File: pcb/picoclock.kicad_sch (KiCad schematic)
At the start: 59 parts, among them J1 UART, J10 USB, J11 Alt Power, J12 PWM, J2 AUDIO, J3 xx, J4 xx, J5 Micro_SD_Card_Det1, J6 USB_C_Receptacle, J7 xx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

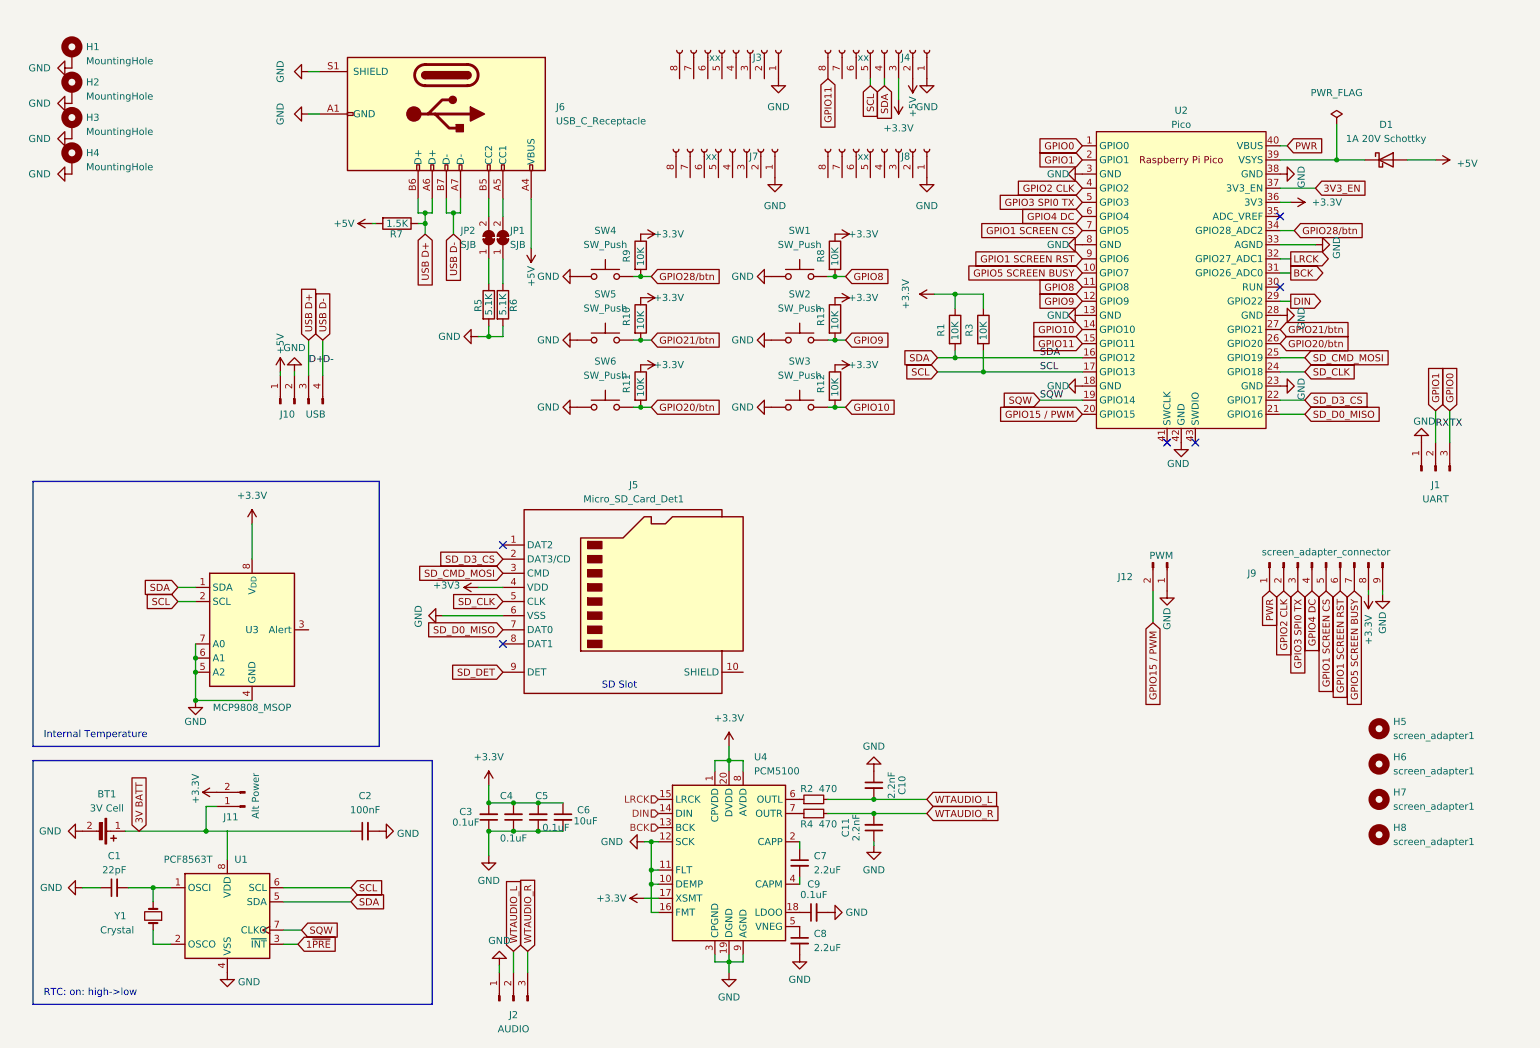
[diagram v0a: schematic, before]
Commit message: [pcb] new GPIO arrangement
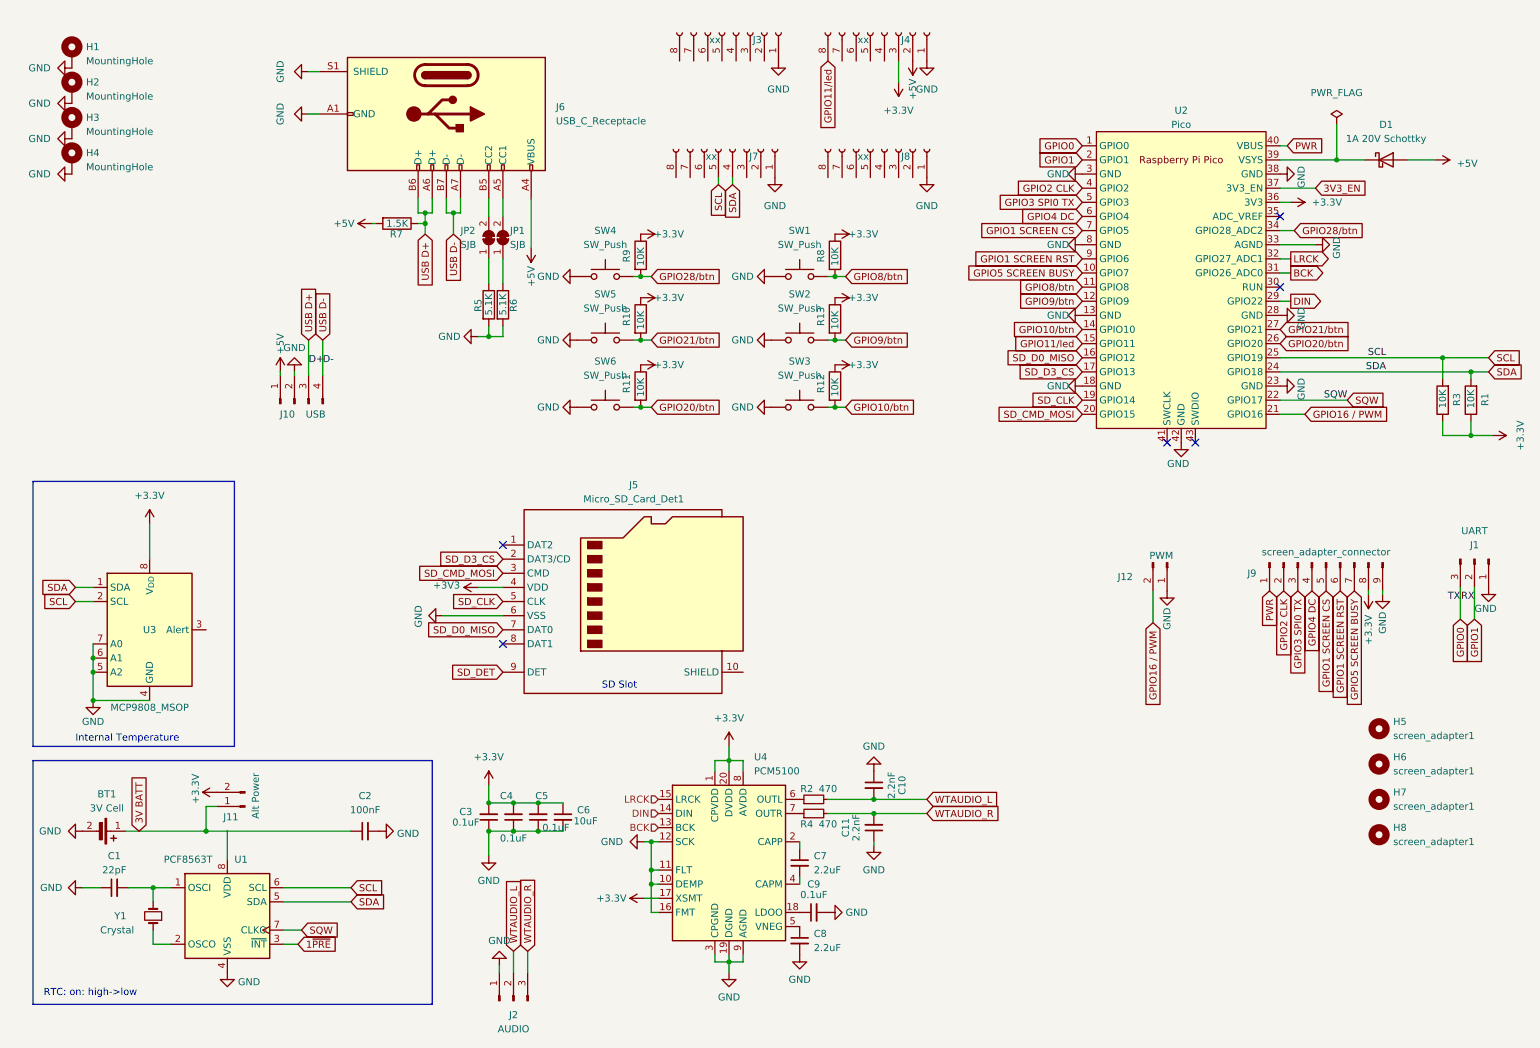
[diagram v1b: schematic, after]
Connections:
- net SCL: now also J7.5 (Pin_5), U2.25 (GPIO19); no longer J4.5 (Pin_5), U2.17 (GPIO13)
- net SDA: now also J7.4 (Pin_4), U2.24 (GPIO18); no longer J4.4 (Pin_4), U2.16 (GPIO12)
- net SD_CLK: now also U2.19 (GPIO14); no longer U2.24 (GPIO18)
- net SD_CMD_MOSI: now also U2.20 (GPIO15); no longer U2.25 (GPIO19)
- net SD_D0_MISO: now also U2.16 (GPIO12); no longer U2.21 (GPIO16)
- net SD_D3_CS: now also U2.17 (GPIO13); no longer U2.22 (GPIO17)
- net SQW: now also U2.22 (GPIO17); no longer U2.19 (GPIO14)
- net GPIO10 renamed GPIO10/btn
- net GPIO11 renamed GPIO11/led
- net GPIO15 / PWM renamed GPIO16 / PWM
- net GPIO16 / PWM: now also U2.21 (GPIO16); no longer U2.20 (GPIO15)
- net GPIO8 renamed GPIO8/btn
- net GPIO9 renamed GPIO9/btn
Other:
- moved on the sheet: J1, J3, J4, U3

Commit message: [pcb] add sdcard, audio amplifier
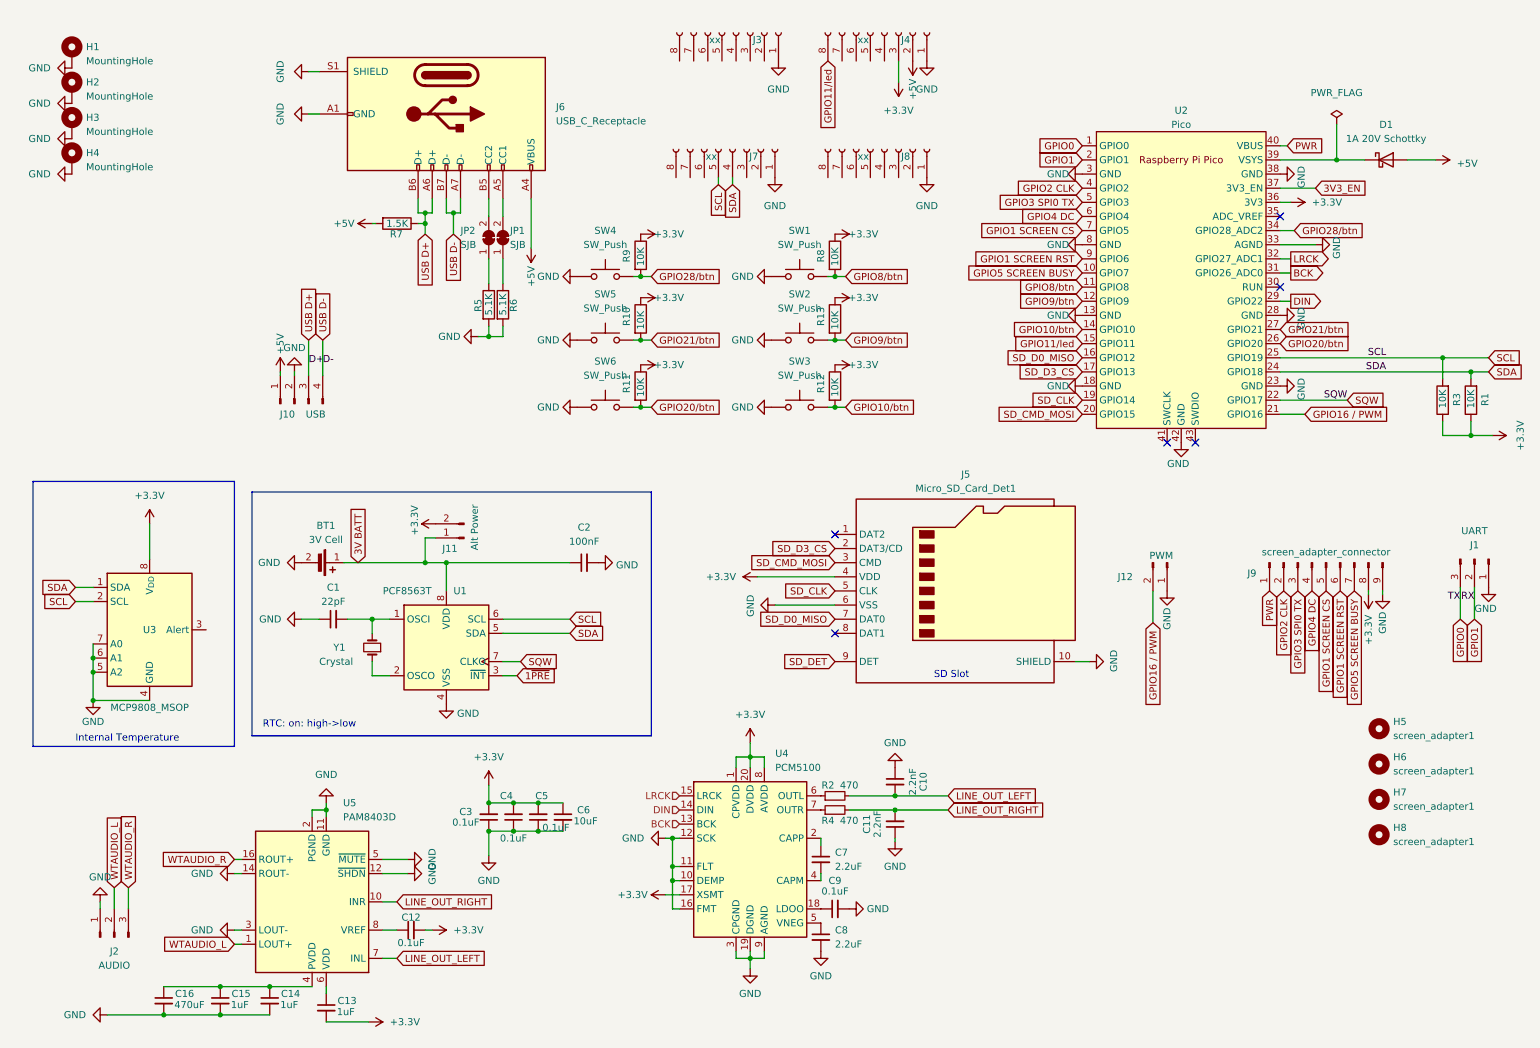
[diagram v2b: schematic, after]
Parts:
- added C12: 0.1uF, Capacitor_SMD:C_0603_1608Metric, symbol Device:C_Small
- added C13, C14, C15: 1uF, Capacitor_SMD:C_0603_1608Metric, symbol Device:C_Small
- added C16: 470uF, Capacitor_SMD:C_0603_1608Metric, symbol Device:C_Small
- added U5: PAM8403D, Package_SO:SOP-16_3.9x9.9mm_P1.27mm, symbol Amplifier_Audio:PAM8403D
- J5: footprint (none) -> Connector_Card:microSD_HC_Hirose_DM3AT-SF-PEJM5
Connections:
- net +3V3 is gone; now on net +3.3V: J5.4 (VDD)
- net +3.3V: now also C12.2, C13.2
- net GND: now also J5.10 (SHIELD), C14.2, C15.2, C16.2, U5.11 (GND), U5.12 (~{SHDN}), U5.14 (ROUT-), U5.15 (PGND), U5.2 (PGND), U5.3 (LOUT-), U5.5 (~{MUTE})
- net WTAUDIO_L: now also U5.1 (LOUT+); no longer C10.2, R2.2
- net WTAUDIO_R: now also U5.16 (ROUT+); no longer C11.2, R4.2
- new net: C13.1, U5.6 (VDD)
- new net: C14.1, C15.1, C16.1, U5.13 (PVDD), U5.4 (PVDD)
- new net: C12.1, U5.8 (VREF)
- new net LINE_OUT_LEFT: C10.2, R2.2, U5.7 (INL)
- new net LINE_OUT_RIGHT: C11.2, R4.2, U5.10 (INR)
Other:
- moved on the sheet: BT1, C1, C10, C11, C2, C7, C8, C9, J11, J2, J5, R2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

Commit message: [pcb] update
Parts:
- added J13: AUDIO, Connector_PinHeader_2.54mm:PinHeader_1x02_P2.54mm_Vertical, symbol Connector:Conn_01x02_Pin
- added J14: SUPPORT, Connector_PinHeader_2.54mm:PinHeader_1x02_P2.54mm_Vertical, symbol Connector:Conn_01x02_Pin
- added R14, R15: 470, Resistor_SMD:R_0603_1608Metric, symbol Device:R_Small
- added U6: MCP23009-SO, Package_SO:SSOP-20_5.3x7.2mm_P0.65mm, symbol MCP23009-E_SO:MCP23009-SO
- added U7: MCP4652T, Package_SO:MSOP-10_3x3mm_P0.5mm, symbol MCP4652:MCP4652T
- J2: footprint Connector_PinHeader_2.54mm:PinHeader_1x03_P2.54mm_Vertical -> Connector_PinHeader_2.54mm:PinHeader_1x02_P2.54mm_Vertical; symbol Connector:Conn_01x03_Pin -> Connector:Conn_01x02_Pin
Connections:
- net +3.3V: now also U6.1 (VDD), U6.6 (~{RESET}), U7.10 (V_{DD})
- net GND: now also U6.18 (VSS), U6.5 (ADDR), U7.1 (A0), U7.4 (V_{SS}), U7.9 (A1); no longer J2.1 (Pin_1), U5.12 (~{SHDN}), U5.14 (ROUT-), U5.3 (LOUT-), U5.5 (~{MUTE})
- net LINE_OUT_LEFT: now also R14.2; no longer U5.7 (INL)
- net LINE_OUT_RIGHT: now also R15.1; no longer U5.10 (INR)
- net SCL: now also U6.3 (SCL), U7.2 (SCL)
- net SDA: now also U6.4 (SDA), U7.3 (SDA)
- net SD_DET: now also U6.10 (GP2)
- net GPIO11/led renamed GPIO11/irq
- net GPIO11/irq: now also U6.7 (INT); no longer J4.8 (Pin_8)
- net WTAUDIO_L renamed AUDIO_OUT_L+
- net AUDIO_OUT_L+: now also J13.2 (Pin_2); no longer J2.2 (Pin_2)
- net WTAUDIO_R renamed AUDIO_OUT_R+
- net AUDIO_OUT_R+: now also J2.2 (Pin_2); no longer J2.3 (Pin_3)
- new net: R15.2, U7.8 (P0B)
- new net: R14.1, U7.5 (P1B)
- new net AUDIO_OUT_L-: J13.1 (Pin_1), U5.3 (LOUT-)
- new net AUDIO_OUT_R-: J2.1 (Pin_1), U5.14 (ROUT-)
- new net GPIO/led: J4.8 (Pin_8), U6.15 (GP7)
- new net LOL_ADJ: U5.7 (INL), U7.7 (P0W)
- new net LOR_ADJ: U5.10 (INR), U7.6 (P1W)
- new net MUTE: U5.12 (~{SHDN}), U5.5 (~{MUTE}), U6.8 (GP0)
- new net SHDN: U6.9 (GP1)
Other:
- moved on the sheet: BT1, C1, C12, C13, C14, C15, C16, C2, C3, C4, C5, C6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

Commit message: [pcb] update/fixes for #prod2
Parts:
- added C17: 100nF, Capacitor_SMD:C_0603_1608Metric, symbol Device:C_Small
- added R16: 10K, Resistor_SMD:R_0603_1608Metric, symbol Device:R
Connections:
- net +3.3V: now also C13.1, C14.1, C15.1, C16.1, U5.13 (PVDD), U5.4 (PVDD), U5.6 (VDD), C17.1, R16.2; no longer C12.2, C13.2
- net GND: now also C12.2, C13.2, C17.2
- net MUTE: now also R16.1
- net PWR: no longer names the net of J9.1 (Pin_1)
- net PWR: no longer U2.40 (VBUS)
- no-connect marks 6 -> 8
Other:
- moved on the sheet: C12, C13, C14, C15, C16, U5
